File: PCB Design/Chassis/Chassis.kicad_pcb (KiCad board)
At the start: 2 copper layers, 55 parts, among them J1 5V voltage regulator, J10 Conn_01x02, J11 Conn_01x02, J12 Conn_01x02, J13 Conn_01x02, J15 Conn_01x02, J2 Conn_01x02, J3 Conn_01x02, J4 Conn_01x02, J5 Conn_01x02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

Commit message: pcb changes
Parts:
- added C1: 470uf, Capacitor_THT:CP_Radial_D10.0mm_P2.50mm, F.Cu at (88.1, 94.5)
- added J14: Conn_01x02, Connector_PinHeader_2.54mm:PinHeader_1x02_P2.54mm_Vertical, F.Cu at (98.6, 86.2)
- added J16: microcontroller extension header, AA_Oscars_Custom:simple 01x06, F.Cu at (136.5, 117.5)
- added J17: Microcontroller extension header, AA_Oscars_Custom:simple 01x12, F.Cu at (101.0, 104.8)
- added J18: Conn_01x02, Connector_PinHeader_2.54mm:PinHeader_1x02_P2.54mm_Vertical, F.Cu at (103.3, 86.2)
- added PS1: RPMGE12-10, AA_Oscars_Custom:CONV_RPMGE12-10, F.Cu at (88.7, 130.0)
- added R14: R, Resistor_THT:R_Axial_DIN0207_L6.3mm_D2.5mm_P5.08mm_Vertical, F.Cu at (98.8, 99.3)
- R10, R11, R12, R13, R2, R3, R4, R5, R6, R7, R8, R9: moved to B.Cu
- moved J9 112.3 mm to (75.0, 56.0), turned to -90 degrees
- moved J10 107.9 mm to (75.0, 65.0), turned to -90 degrees
- moved J11 104.9 mm to (75.0, 74.0), turned to -90 degrees
- moved J12 103.4 mm to (75.0, 82.9), turned to -90 degrees
- moved D8 89.3 mm to (93.8, 54.7), turned to 90 degrees
- moved A1 84.1 mm to (128.9, 130.2), turned to 180 degrees
- moved D9 82.4 mm to (93.8, 65.7), turned to 90 degrees
- moved D10 78.1 mm to (93.8, 76.3), turned to 90 degrees
- moved D11 76.6 mm to (93.8, 86.8), turned to 90 degrees
- moved Q5 66.2 mm to (104.5, 53.8), turned to 135 degrees
- moved Q13 64.9 mm to (131.8, 63.0)
- moved Q7 62.8 mm to (131.8, 75.4)
- moved D1 62.2 mm to (139.4, 102.5)
- moved Q4 61.4 mm to (115.9, 53.7), turned to 135 degrees
- moved J1 60.4 mm to (84.2, 93.2), turned to 90 degrees
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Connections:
- A1 pad 1: unconnected-(A1-~{RESET}-Pad1) -> Net-(A1-~{RESET})
- A1 pad 11: unconnected-(A1-SCK-Pad11) -> Net-(A1-SCK)
- A1 pad 12: unconnected-(A1-MOSI-Pad12) -> Net-(A1-MOSI)
- A1 pad 13: unconnected-(A1-MISO-Pad13) -> Net-(A1-MISO)
- A1 pad 14: unconnected-(A1-RX-Pad14) -> Net-(A1-RX)
- A1 pad 15: unconnected-(A1-TX-Pad15) -> Net-(A1-TX)
- A1 pad 17: unconnected-(A1-SDA-Pad17) -> Net-(A1-SDA)
- A1 pad 18: unconnected-(A1-SCL-Pad18) -> Net-(A1-SCL)
- A1 pad 2: unconnected-(A1-3V3-Pad2) -> Net-(A1-3V3)
- A1 pad 27: unconnected-(A1-EN-Pad27) -> Net-(A1-EN)
- A1 pad 28: unconnected-(A1-VBAT-Pad28) -> Net-(A1-VBAT)
- A1 pad 3: unconnected-(A1-AREF-Pad3) -> Net-(A1-AREF)
- Q1 pad 1: Net-(D1-A) -> Net-(Q1-G)
- Q1 pad 2: Net-(Q1-G) -> Net-(D1-A)
- Q10 pad 1: Net-(D10-A) -> Net-(Q10-G)
- Q10 pad 2: Net-(Q10-G) -> Net-(D10-A)
- Q11 pad 1: Net-(D11-A) -> Net-(Q11-G)
- Q11 pad 2: Net-(Q11-G) -> Net-(D11-A)
- Q12 pad 1: Net-(D12-A) -> Net-(Q12-G)
- Q12 pad 2: Net-(Q12-G) -> Net-(D12-A)
- Q13 pad 1: Net-(D13-A) -> Net-(Q13-G)
- Q13 pad 2: Net-(Q13-G) -> Net-(D13-A)
- Q13 pad 3: unconnected-(Q13-S-Pad3) -> gnd
- Q2 pad 1: Net-(D2-A) -> Net-(Q2-G)
- Q2 pad 2: Net-(Q2-G) -> Net-(D2-A)
- Q3 pad 1: Net-(D3-A) -> Net-(Q3-G)
- Q3 pad 2: Net-(Q3-G) -> Net-(D3-A)
- Q4 pad 1: Net-(D4-A) -> Net-(Q4-G)
- Q4 pad 2: Net-(Q4-G) -> Net-(D4-A)
- Q5 pad 1: Net-(D5-A) -> Net-(Q5-G)
- Q5 pad 2: Net-(Q5-G) -> Net-(D5-A)
- Q6 pad 1: Net-(D6-A) -> Net-(Q6-G)
- Q6 pad 2: Net-(Q6-G) -> Net-(D6-A)
- Q7 pad 1: Net-(D7-A) -> Net-(Q7-G)
- Q7 pad 2: Net-(Q7-G) -> Net-(D7-A)
- Q8 pad 1: Net-(D8-A) -> Net-(Q8-G)
- Q8 pad 2: Net-(Q8-G) -> Net-(D8-A)
- Q9 pad 1: Net-(D9-A) -> Net-(Q9-G)
- Q9 pad 2: Net-(Q9-G) -> Net-(D9-A)
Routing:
- net pos: track 0.00 -> 330.7 mm
- net gnd: track 0.00 -> 225.6 mm
- net Net-(A1-A1): track 0.00 -> 61.7 mm, vias 0 -> 1
- net Net-(A1-D4): track 0.00 -> 58.7 mm, vias 0 -> 1
- net Net-(A1-D6): track 0.00 -> 58.3 mm, vias 0 -> 2
- net Net-(A1-D3): track 0.00 -> 55.2 mm
- net Net-(A1-A2): track 0.00 -> 52.8 mm, vias 0 -> 1
- net Net-(A1-A0): track 0.00 -> 52.1 mm, vias 0 -> 1
- net Net-(A1-D5): track 0.00 -> 49.4 mm
- net Net-(A1-A3): track 0.00 -> 48.2 mm, vias 0 -> 1
- net Net-(A1-D2): track 0.00 -> 45.5 mm
- net Net-(A1-D1): track 0.00 -> 43.5 mm
- net Net-(A1-A5): track 0.00 -> 43.4 mm
- net Net-(A1-A4): track 0.00 -> 40.3 mm, vias 0 -> 1
- net Net-(A1-USB): track 0.00 -> 37.4 mm
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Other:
- board outline added: 87.9 x 134.6 mm

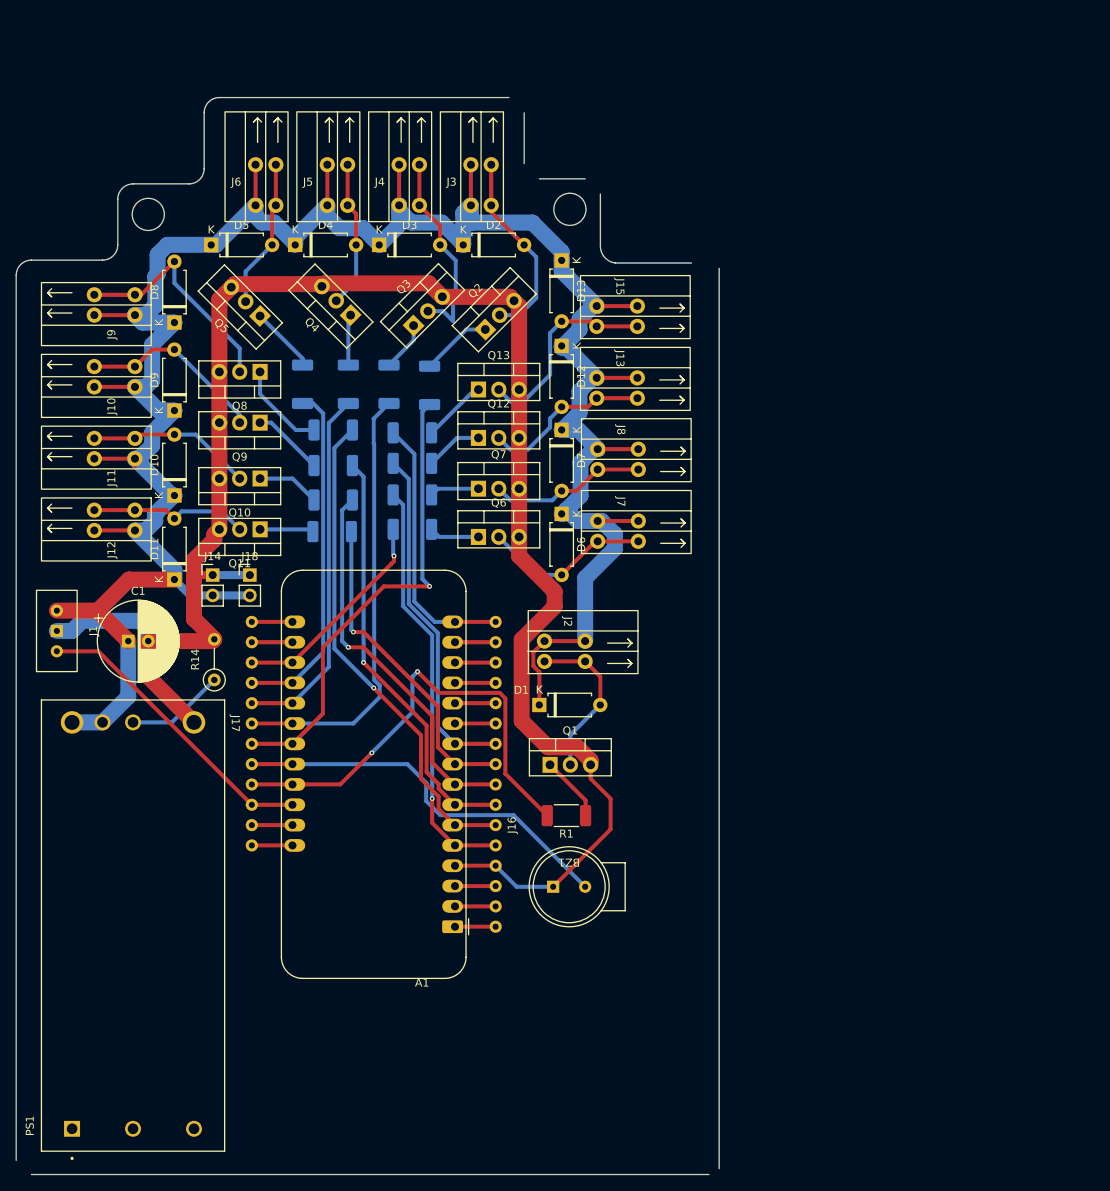
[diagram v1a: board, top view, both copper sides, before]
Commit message: small change to solenoid script
more real application func
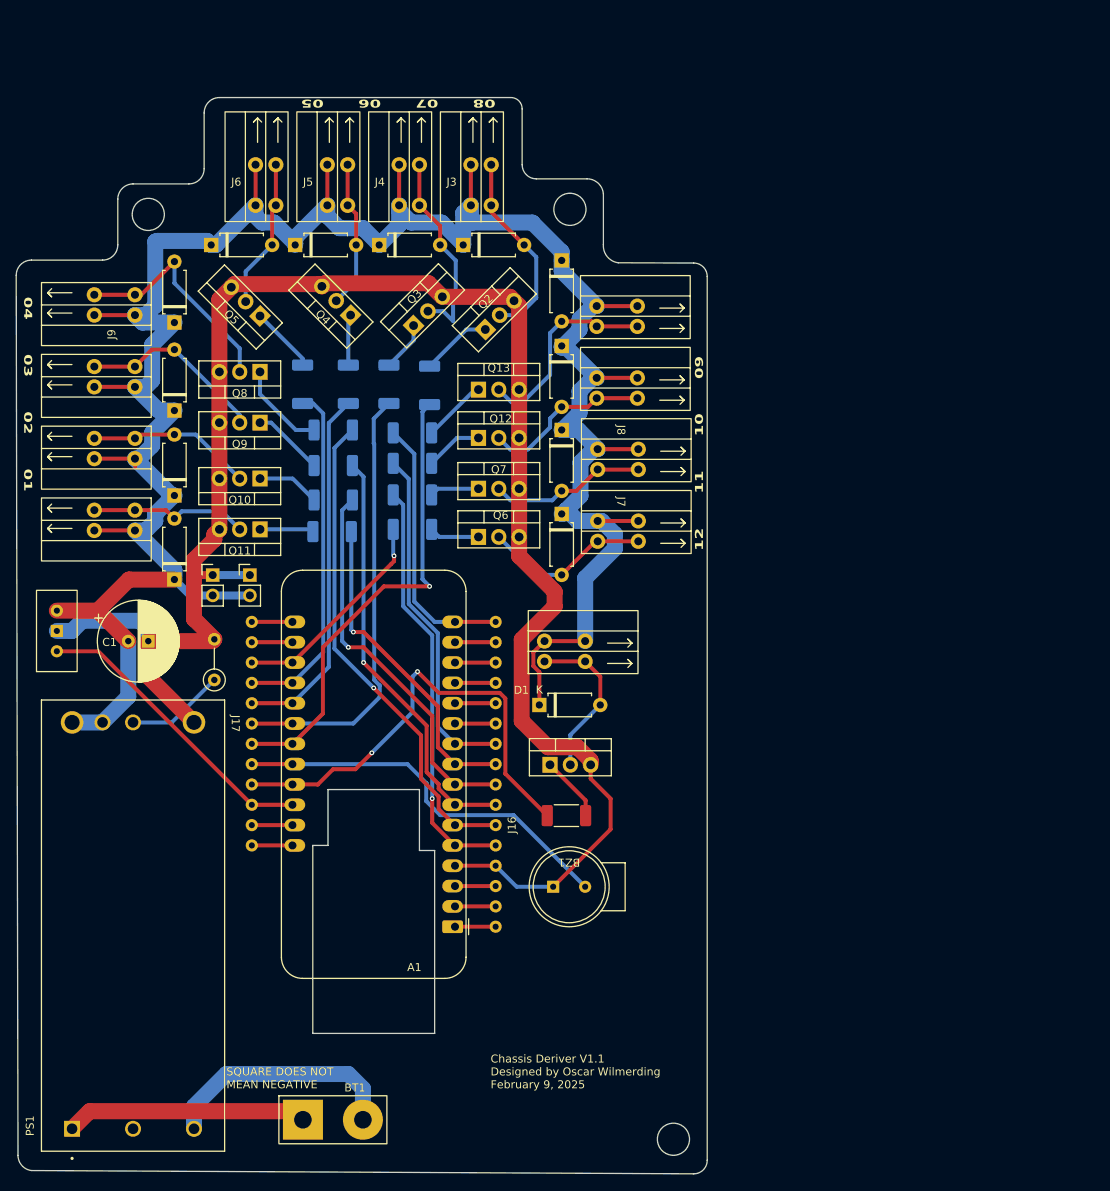
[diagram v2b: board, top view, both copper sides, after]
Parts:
- added BT1: Battery_Cell, AA_Oscars_Custom:Ec5 pigtail, F.Cu at (112.4, 154.3)
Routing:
- net Net-(BT1--): track 0.00 -> 30.2 mm
- net Net-(BT1-+): track 0.00 -> 30.2 mm
- net pos: track 330.7 -> 332.2 mm
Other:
- board size 87.9 x 134.6 mm -> 86.4 x 134.5 mm
- board text added: "04 03 02 01"
- board text added: "08 07 06 05"
- board text added: "12 11 10 09"
- board text added: "Chassis Deriver V1.1 Designed by Oscar Wilmerding February 9, 2025"
- board text added: "SQUARE DOES NOT MEAN NEGATIVE"
